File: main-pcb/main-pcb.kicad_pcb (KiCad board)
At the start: 10 copper layers, 12.8 x 6.5 mm, 428 parts, among them J1 CONN_01X03, J10 CONN_DUMPTRUCK_HOST, J11 CONN_01X03, J12 PMOD_HOST, J13 PMOD_HOST, J14 USB_C_Receptacle_USB2.0, J2 CORTEX_DEBUG_ETM, J3 XILINX_JTAG, J4 CORTEX_DEBUG_ETM, J5 CONN_01X03, J6 0826-1G1T-23-F, J7 CONN_DUMPTRUCK_HOST, J8 CONN_DUMPTRUCK_HOST, J9 CONN_DUMPTRUCK_HOST, M1 MECHANICAL, M2 SCREWHOLE, M3 SCREWHOLE, M4 SCREWHOLE, M5 SCREWHOLE, M6 MECHANICAL, M7 MECHANICAL, M8 MECHANICAL, M9 MECHANICAL, Q1 SSM6N58NU, SW1 SWITCH, SW2 SWITCH, U1 XC7S100-1FGGA484C, U10 NCP45525IMNTWG-H, U11 LTC3374-QFN, U12 AT24MAC402, U13 ECS-1612MV-250-CN, U14 STM32H735-UFBGA176-25, U15 S27KL0642GABHB020, U16 ECS-1612MV-250-CN, U17 S27KS0642GABHI030, U18 ECS-1612MV-250-CN, U19 INA230, U2 STM32L431-QFN48, U20 KSZ9031RN, U21 RCLAMP0514M, U22 RCLAMP0514M, U23 NCP45525IMNTWG-H, U24 IS25WP256D-JLLE, U25 INA230, U26 74LVC1T45, U27 NCP45525IMNTWG-H, U28 INA230, U29 NCP45525IMNTWG-H, U3 INA230, U30 INA230, U31 NCP45525IMNTWG-H, U32 INA230, U33 19-C47/RSGHBHC-5V01/2T, U34 19-C47/RSGHBHC-5V01/2T, U35 19-C47/RSGHBHC-5V01/2T, U36 19-C47/RSGHBHC-5V01/2T, U37 19-C47/RSGHBHC-5V01/2T, U38 19-C47/RSGHBHC-5V01/2T, U39 NCP45525IMNTWG-H, U4 INA230, U5 INA230, U6 INA230, U7 INA230, U8 INA230, U9 INA230

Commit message: Finished schematic review
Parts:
- added C208: 0.47 uF, azonenberg_pcb:EIA_0402_CAP_NOSILK, F.Cu at (38.3, 102.3)
- added TP18: GROUND, azonenberg_pcb:TESTPOINT_SMT_KEYSTONE_5016, F.Cu at (116.9, 43.2)
- added TP19: GROUND, azonenberg_pcb:TESTPOINT_SMT_KEYSTONE_5016, F.Cu at (116.9, 47.7)
- added TP20: GROUND, azonenberg_pcb:TESTPOINT_SMT_KEYSTONE_5016, F.Cu at (116.9, 52.1)
- R100, R96, R98: value 10K -> DNP
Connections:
- C100 pad 1: /Power supply/VBUS_SHOUT -> /VBUS_SHOUT
- C101 pad 1: /Power supply/VBUS_SHOUT -> /VBUS_SHOUT
- C166 pad 1: /Power supply/VBUS_SHOUT -> /VBUS_SHOUT
- C167 pad 1: /Power supply/VBUS_SHOUT -> /VBUS_SHOUT
- C169 pad 1: /Power supply/VBUS_SHOUT -> /VBUS_SHOUT
- C170 pad 1: /Power supply/VBUS_SHOUT -> /VBUS_SHOUT
- C171 pad 1: /Power supply/VBUS_SHOUT -> /VBUS_SHOUT
- C172 pad 1: /Power supply/VBUS_SHOUT -> /VBUS_SHOUT
- C173 pad 1: /Power supply/VBUS_SHOUT -> /VBUS_SHOUT
- C198 pad 1: /VBUS -> /VBUS_SHOUT
- C200 pad 1: /VBUS -> /VBUS_SHOUT
- C202 pad 1: /VBUS -> /VBUS_SHOUT
- C203 pad 1: /VBUS -> /VBUS_SHOUT
- C204 pad 1: /VBUS -> /VBUS_SHOUT
- C205 pad 1: /VBUS -> /VBUS_SHOUT
- C206 pad 1: /VBUS -> /VBUS_SHOUT
- C91 pad 1: /Power supply/VBUS_SHOUT -> /VBUS_SHOUT
- C93 pad 1: /Power supply/VBUS_SHOUT -> /VBUS_SHOUT
- C94 pad 1: /Power supply/VBUS_SHOUT -> /VBUS_SHOUT
- C96 pad 1: /Power supply/VBUS_SHOUT -> /VBUS_SHOUT
- C97 pad 1: /Power supply/VBUS_SHOUT -> /VBUS_SHOUT
- C98 pad 1: /Power supply/VBUS_SHOUT -> /VBUS_SHOUT
- J14 pad A6: Net-(J14-D+-PadA6) -> unconnected-(J14-D+-PadA6)
- J14 pad A7: Net-(J14-D--PadA7) -> unconnected-(J14-D--PadA7)
- J14 pad B6: Net-(J14-D+-PadA6) -> unconnected-(J14-D+-PadB6)
- J14 pad B7: Net-(J14-D--PadA7) -> unconnected-(J14-D--PadB7)
- R9 pad 1: /Power supply/VBUS_SHOUT -> /VBUS_SHOUT
- TP2 pad 1: /Power supply/VBUS_SHOUT -> /VBUS_SHOUT
- U11 pad 11: /Power supply/VBUS_SHOUT -> /VBUS_SHOUT
- U11 pad 13: /Power supply/VBUS_SHOUT -> /VBUS_SHOUT
- U11 pad 17: /Power supply/VBUS_SHOUT -> /VBUS_SHOUT
- U11 pad 2: /Power supply/VBUS_SHOUT -> /VBUS_SHOUT
- U11 pad 21: /Power supply/VBUS_SHOUT -> /VBUS_SHOUT
- U11 pad 24: /Power supply/VBUS_SHOUT -> /VBUS_SHOUT
- U11 pad 27: /Power supply/VBUS_SHOUT -> /VBUS_SHOUT
- U11 pad 30: /Power supply/VBUS_SHOUT -> /VBUS_SHOUT
- U11 pad 31: /Power supply/VBUS_SHOUT -> /VBUS_SHOUT
- U11 pad 35: /Power supply/VBUS_SHOUT -> /VBUS_SHOUT
- U11 pad 5: /Power supply/VBUS_SHOUT -> /VBUS_SHOUT
- U11 pad 6: /Power supply/VBUS_SHOUT -> /VBUS_SHOUT
- U11 pad 8: /Power supply/VBUS_SHOUT -> /VBUS_SHOUT
- U26 pad 6: /VBUS -> /VBUS_SHOUT
- U3 pad 11: /Power supply/VBUS_SHOUT -> /VBUS_SHOUT
- U3 pad 12: /Power supply/VBUS_SHOUT -> /VBUS_SHOUT
- U33 pad 2: /VBUS -> /VBUS_SHOUT
- U34 pad 2: /VBUS -> /VBUS_SHOUT
- U35 pad 2: /VBUS -> /VBUS_SHOUT
- U36 pad 2: /VBUS -> /VBUS_SHOUT
- U37 pad 2: /VBUS -> /VBUS_SHOUT
- U38 pad 2: /VBUS -> /VBUS_SHOUT

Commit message: First DUT socket fully routed
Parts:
- added C209: 47 uF, azonenberg_pcb:EIA_1210_CAP_NOSILK, F.Cu at (265.1, 66.9)
- added C210: 4.7 uF, azonenberg_pcb:EIA_0603_CAP_NOSILK, F.Cu at (264.2, 69.8)
- added C211: 4.7 uF, azonenberg_pcb:EIA_0603_CAP_NOSILK, F.Cu at (264.2, 71.6)
- added C212: 0.47 uF, azonenberg_pcb:EIA_0402_CAP_NOSILK, F.Cu at (261.3, 65.7)
- added C213: 0.47 uF, azonenberg_pcb:EIA_0402_CAP_NOSILK, F.Cu at (261.3, 67.2)
- added C214: 0.47 uF, azonenberg_pcb:EIA_0402_CAP_NOSILK, F.Cu at (261.3, 68.7)
- added C215: 0.47 uF, azonenberg_pcb:EIA_0402_CAP_NOSILK, F.Cu at (261.3, 70.2)
- C26, C27, C28, C29, C30, C31, C32, C33, C34, C40, C41, C42, C43, C44, C45, C55, C56, C57, C58, C59, C60, C62, C63, C67, C68, C69, C70, C75, C76, C77, C85, C86, C87, C88, C89, C90: moved to B.Cu
- moved C100 149.5 mm to (215.9, 41.9)
- moved C135 149.5 mm to (215.9, 44.5)
- moved C166 149.5 mm to (215.9, 47.1)
- moved C169 149.5 mm to (215.9, 49.7)
- moved C95 149.5 mm to (215.9, 39.3)
- moved C1 149.5 mm to (199.6, 38.8)
- moved C10 149.5 mm to (199.6, 50.8)
- moved C101 149.5 mm to (202.1, 46.3)
- moved C104 149.5 mm to (176.9, 77.2)
- moved C105 149.5 mm to (176.9, 79.0)
- moved C106 149.5 mm to (199.6, 60.9)
- moved C107 149.5 mm to (199.6, 63.5)
- moved C108 149.5 mm to (176.9, 80.8)
- moved C11 149.5 mm to (199.6, 52.3)
- moved C110 149.5 mm to (176.9, 82.6)
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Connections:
- U1 pad H2: /1V8 VCCIO socket/DUT_GPIO2 -> /1V8 VCCIO socket/DUT_GPIO40
- U1 pad H3: /1V8 VCCIO socket/DUT_GPIO4 -> /1V8 VCCIO socket/DUT_GPIO36
- U1 pad H4: /1V8 VCCIO socket/DUT_GPIO3 -> /1V8 VCCIO socket/DUT_GPIO38
- U1 pad H5: /1V8 VCCIO socket/DUT_GPIO10 -> /1V8 VCCIO socket/DUT_GPIO24
- U1 pad H6: /1V8 VCCIO socket/DUT_GPIO9 -> /1V8 VCCIO socket/DUT_GPIO26
- U1 pad H7: /1V8 VCCIO socket/DUT_GPIO0 -> /1V8 VCCIO socket/DUT_GPIO22
- U1 pad J1: /1V8 VCCIO socket/DUT_GPIO6 -> /1V8 VCCIO socket/DUT_GPIO46
- U1 pad J2: /1V8 VCCIO socket/DUT_GPIO5 -> /1V8 VCCIO socket/DUT_GPIO48
- U1 pad J3: /1V8 VCCIO socket/DUT_GPIO1 -> /1V8 VCCIO socket/DUT_GPIO34
- U1 pad J6: /1V8 VCCIO socket/DUT_GPIO12 -> /1V8 VCCIO socket/DUT_GPIO20
- U1 pad J7: /1V8 VCCIO socket/DUT_GPIO14 -> /1V8 VCCIO socket/DUT_GPIO18
- U1 pad J8: /1V8 VCCIO socket/DUT_GPIO13 -> /1V8 VCCIO socket/DUT_GPIO14
- U1 pad K1: /1V8 VCCIO socket/DUT_GPIO28 -> /1V8 VCCIO socket/DUT_GPIO42
- U1 pad K2: /1V8 VCCIO socket/DUT_GPIO8 -> /1V8 VCCIO socket/DUT_GPIO44
- U1 pad K3: /1V8 VCCIO socket/DUT_GPIO7 -> /1V8 VCCIO socket/DUT_GPIO41
- U1 pad K4: /1V8 VCCIO socket/DUT_GPIO20 -> /1V8 VCCIO socket/DUT_GPIO30
- U1 pad K5: /1V8 VCCIO socket/DUT_GPIO18 -> /1V8 VCCIO socket/DUT_GPIO32
- U1 pad K6: /1V8 VCCIO socket/DUT_GPIO11 -> /1V8 VCCIO socket/DUT_GPIO16
- U1 pad K8: /1V8 VCCIO socket/DUT_GPIO22 -> /1V8 VCCIO socket/DUT_GPIO12
- U1 pad L1: /1V8 VCCIO socket/DUT_GPIO27 -> /1V8 VCCIO socket/DUT_GPIO43
- U1 pad L4: /1V8 VCCIO socket/DUT_GPIO19 -> /1V8 VCCIO socket/DUT_GPIO28
- U1 pad L5: /1V8 VCCIO socket/DUT_GPIO17 -> /1V8 VCCIO socket/DUT_GPIO1
- U1 pad L6: /1V8 VCCIO socket/DUT_GPIO16 -> /1V8 VCCIO socket/DUT_GPIO0
- U1 pad L7: /1V8 VCCIO socket/DUT_GPIO15 -> /1V8 VCCIO socket/DUT_GPIO3
- U1 pad L8: /1V8 VCCIO socket/DUT_GPIO21 -> /1V8 VCCIO socket/DUT_GPIO10
- U1 pad M1: /1V8 VCCIO socket/DUT_GPIO30 -> /1V8 VCCIO socket/DUT_GPIO47
- U1 pad M2: /1V8 VCCIO socket/DUT_GPIO29 -> /1V8 VCCIO socket/DUT_GPIO49
- U1 pad M3: /1V8 VCCIO socket/DUT_GPIO26 -> /1V8 VCCIO socket/DUT_GPIO45
- U1 pad M4: /1V8 VCCIO socket/DUT_GPIO25 -> /1V8 VCCIO socket/DUT_GPIO27
- U1 pad M5: /1V8 VCCIO socket/DUT_GPIO40 -> /1V8 VCCIO socket/DUT_GPIO25
- U1 pad M7: /1V8 VCCIO socket/DUT_GPIO24 -> /1V8 VCCIO socket/DUT_GPIO5
- U1 pad M8: /1V8 VCCIO socket/DUT_GPIO23 -> /1V8 VCCIO socket/DUT_GPIO8
- U1 pad N1: /1V8 VCCIO socket/DUT_GPIO34 -> /1V8 VCCIO socket/DUT_GPIO39
- U1 pad N3: /1V8 VCCIO socket/DUT_GPIO32 -> /1V8 VCCIO socket/DUT_GPIO31
- U1 pad N4: /1V8 VCCIO socket/DUT_GPIO31 -> /1V8 VCCIO socket/DUT_GPIO29
- U1 pad N5: /1V8 VCCIO socket/DUT_GPIO39 -> /1V8 VCCIO socket/DUT_GPIO23
- U1 pad N6: /1V8 VCCIO socket/DUT_GPIO42 -> /1V8 VCCIO socket/DUT_GPIO17
- U1 pad N7: /1V8 VCCIO socket/DUT_GPIO44 -> /1V8 VCCIO socket/DUT_GPIO7
- U1 pad N8: /1V8 VCCIO socket/DUT_GPIO38 -> /1V8 VCCIO socket/DUT_GPIO6
- U1 pad P1: /1V8 VCCIO socket/DUT_GPIO33 -> /1V8 VCCIO socket/DUT_GPIO35
- U1 pad P2: /1V8 VCCIO socket/DUT_GPIO36 -> /1V8 VCCIO socket/DUT_GPIO37
- U1 pad P3: /1V8 VCCIO socket/DUT_GPIO35 -> /1V8 VCCIO socket/DUT_GPIO33
- U1 pad P6: /1V8 VCCIO socket/DUT_GPIO41 -> /1V8 VCCIO socket/DUT_GPIO13
- U1 pad P7: /1V8 VCCIO socket/DUT_GPIO43 -> /1V8 VCCIO socket/DUT_GPIO15
- U1 pad P8: /1V8 VCCIO socket/DUT_GPIO37 -> /1V8 VCCIO socket/DUT_GPIO4
- U1 pad R3: /1V8 VCCIO socket/DUT_GPIO49 -> /1V8 VCCIO socket/DUT_GPIO19
- U1 pad R4: /1V8 VCCIO socket/DUT_GPIO48 -> /1V8 VCCIO socket/DUT_GPIO21
- U1 pad R5: /1V8 VCCIO socket/DUT_GPIO47 -> /1V8 VCCIO socket/DUT_GPIO9
- U1 pad R6: /1V8 VCCIO socket/DUT_GPIO46 -> /1V8 VCCIO socket/DUT_GPIO11
- U1 pad R7: /1V8 VCCIO socket/DUT_GPIO45 -> /1V8 VCCIO socket/DUT_GPIO2
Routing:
- net /GND: track 0.00 -> 333.5 mm, vias 0 -> 115
- net /3V3: track 0.00 -> 81.4 mm, vias 0 -> 7
- net /1V8: track 0.00 -> 60.9 mm, vias 0 -> 18
- net /1V8 VCCIO socket/DUT_GPIO2: track 0.00 -> 46.2 mm, vias 0 -> 2
- net /1V8 VCCIO socket/DUT_GPIO4: track 0.00 -> 45.9 mm, vias 0 -> 2
- net /1V8 VCCIO socket/DUT_GPIO0: track 0.00 -> 41.6 mm, vias 0 -> 2
- net /1V8 VCCIO socket/DUT_GPIO3: track 0.00 -> 40.6 mm, vias 0 -> 2
- net /1V8 VCCIO socket/DUT_GPIO6: track 0.00 -> 40.6 mm, vias 0 -> 2
- net /1V8 VCCIO socket/DUT_GPIO1: track 0.00 -> 39.9 mm, vias 0 -> 2
- net /1V8 VCCIO socket/DUT_GPIO8: track 0.00 -> 39.4 mm, vias 0 -> 2
- net /1V8 VCCIO socket/DUT_GPIO5: track 0.00 -> 39.1 mm, vias 0 -> 2
- net /1V8 VCCIO socket/DUT_GPIO10: track 0.00 -> 37.9 mm, vias 0 -> 2
- net /1V8 VCCIO socket/DUT_GPIO7: track 0.00 -> 37.2 mm, vias 0 -> 2
- net /1V8 VCCIO socket/DUT_GPIO12: track 0.00 -> 36.4 mm, vias 0 -> 2
- net /1V8 VCCIO socket/DUT_GPIO11: track 0.00 -> 36.0 mm, vias 0 -> 2
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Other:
- board size 12.8 x 6.5 mm -> 133 x 90 mm

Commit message: Continued initial layout of 1.8V bank
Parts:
- C188, C189, C192, R98: moved to B.Cu
- moved C191 172.1 mm to (28.8, 79.5)
- moved U30 172.1 mm to (32.4, 80.8)
- moved C190 165.9 mm to (45.0, 74.0), turned to 180 degrees
- moved U29 162.0 mm to (48.2, 74.0), turned to 180 degrees
- moved C192 159.2 mm to (44.8, 81.0), turned to -90 degrees
- moved R99 157.4 mm to (46.0, 76.0), turned to 90 degrees
- moved C189 155.9 mm to (47.0, 73.2), turned to 90 degrees
- moved C188 153.1 mm to (49.5, 73.2), turned to 90 degrees
- moved R98 152.4 mm to (51.2, 74.7), turned to -90 degrees
- moved J2 81.5 mm to (132.5, 111.0)
- moved J12 54.8 mm to (109.7, 31.3), turned to 180 degrees
- moved J6 51.1 mm to (132.0, 36.5), turned to 0 degrees
- moved J4 20.0 mm to (91.0, 31.0)
- moved U21 19.3 mm to (134.5, 63.0), turned to 0 degrees
- moved U2 17.3 mm to (142.5, 81.5)
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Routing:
- net /1V8: track 60.9 -> 102.2 mm, vias 18 -> 22
- net /GND: track 333.5 -> 348.5 mm, vias 115 -> 123
- net /1V8 VCCIO socket/DUT_VCCIO_SHIN: track 0.00 -> 5.16 mm
- net /DUT_VCCIO_EN: track 0.00 -> 2.00 mm, vias 0 -> 1
- net /3V3: track 81.4 -> 82.7 mm, vias 7 -> 8
- net /1V8 VCCIO socket/DUT_VCCIO: track 6.40 -> 7.59 mm, vias 2 -> 0
- net /DUT_VDD: track 12.5 -> 13.4 mm, vias 4 -> 6
- net Net-(U29-SR): track 0.00 -> 0.25 mm, vias 0 -> 1
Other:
- board size 133 x 90 mm -> 123 x 90 mm

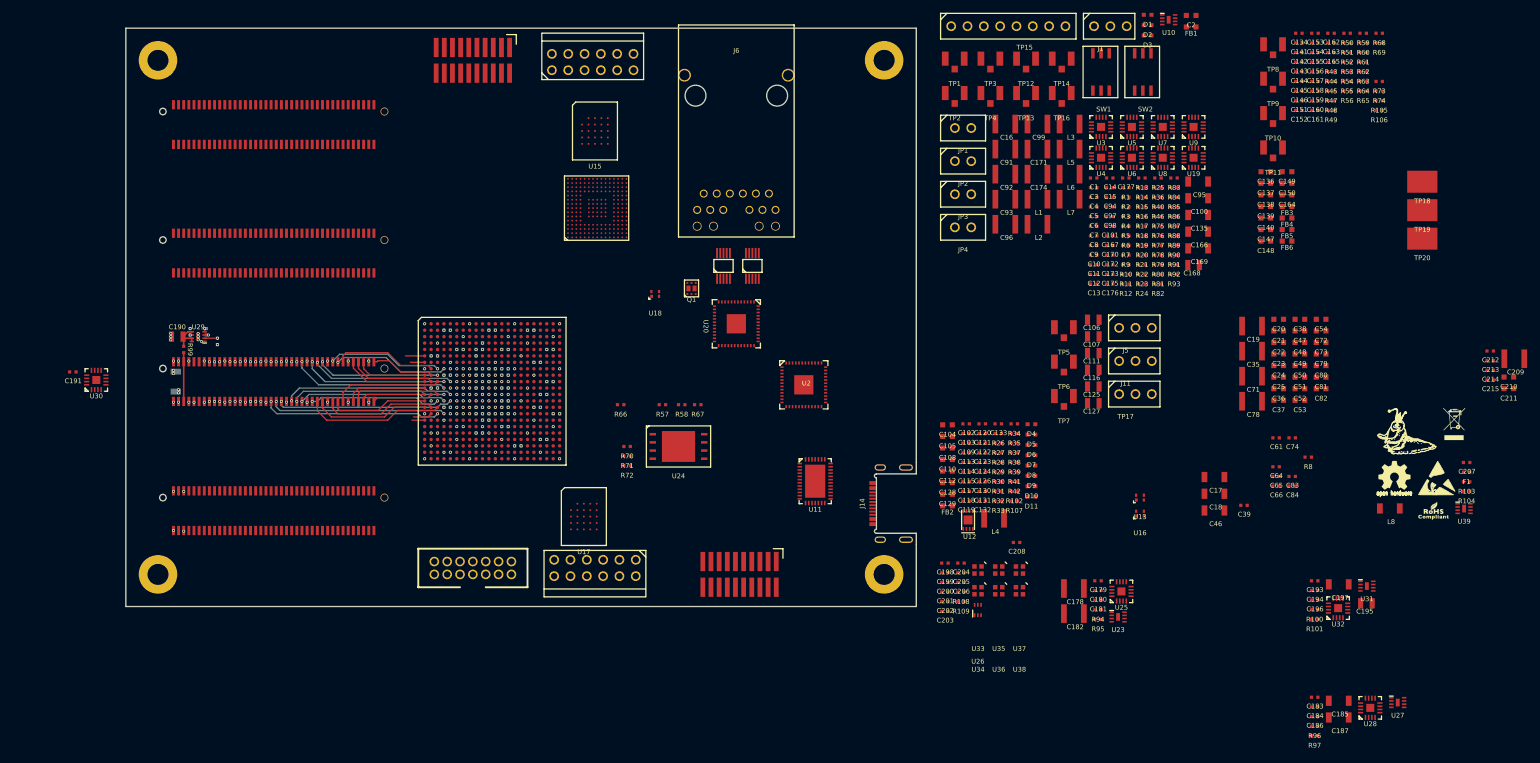
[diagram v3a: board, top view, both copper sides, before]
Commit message: Continued layout mostly of DUT connectors
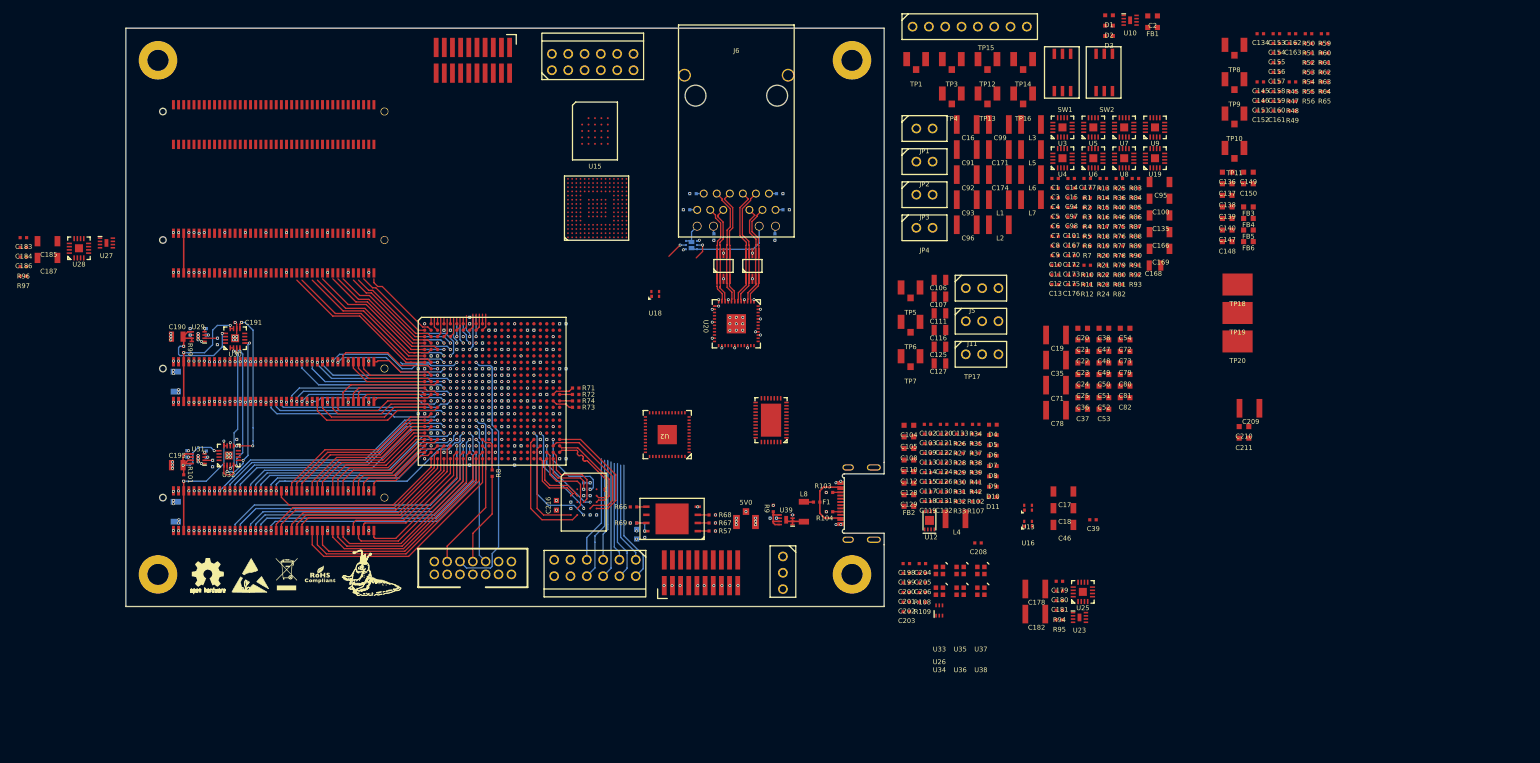
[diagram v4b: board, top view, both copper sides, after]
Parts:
- added C216: 4.7 uF, azonenberg_pcb:EIA_0603_CAP_NOSILK, F.Cu at (104.0, 100.2)
- added C217: 0.47 uF, azonenberg_pcb:EIA_0402_CAP_NOSILK, B.Cu at (108.8, 98.8)
- added C218: 0.47 uF, azonenberg_pcb:EIA_0402_CAP_NOSILK, B.Cu at (109.8, 101.8)
- added C219: 0.47 uF, azonenberg_pcb:EIA_0402_CAP_NOSILK, B.Cu at (106.2, 100.2)
- C141, C142, C143, C144, C164, C165, C193, C194, C196, C197, C207, C212, C213, C214, C215, C61, C64, C65, C66, C74, C83, C84, Q1, R100, R105, R106, R43, R44, R58, R70: moved to B.Cu
- R2, R3: value TBD -> 33K
- R29, R30, R31, R33, R34, R37, R38, R39: value 470 -> 33K
- R4: value TBD -> 4.7K
- moved U27 213.3 mm to (34.0, 59.4)
- moved U28 213.3 mm to (29.7, 60.2)
- moved C183 213.3 mm to (21.1, 58.6)
- moved C184 213.3 mm to (21.1, 60.1)
- moved C185 213.3 mm to (24.8, 59.1)
- moved C186 213.3 mm to (21.1, 61.6)
- moved C187 213.3 mm to (24.8, 61.7)
- moved R96 213.3 mm to (21.1, 63.1)
- moved R97 213.3 mm to (21.1, 64.6)
- moved C195 186.3 mm to (45.0, 94.0), turned to 180 degrees
- moved M7 185.3 mm to (49.8, 110.7)
- moved M6 185.3 mm to (56.5, 111.2)
- moved M9 183.2 mm to (62.0, 111.0)
- moved U31 183.0 mm to (48.2, 93.0), turned to 180 degrees
- moved C197 181.4 mm to (44.8, 101.2), turned to -90 degrees
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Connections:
- U1 pad AA1: /1V2 VCCIO socket/DUT_GPIO34 -> /1V2 VCCIO socket/DUT_GPIO46
- U1 pad AA10: /1V2 VCCIO socket/DUT_GPIO43 -> /1V2 VCCIO socket/DUT_GPIO33
- U1 pad AA2: /1V2 VCCIO socket/DUT_GPIO33 -> /1V2 VCCIO socket/DUT_GPIO48
- U1 pad AA20: /Ethernet/FPGA_RAM_DQ6 -> /Ethernet/FPGA_RAM_DQ1
- U1 pad AA21: /Ethernet/ETH_LED2_N_1V8_INV -> /Ethernet/FPGA_RAM_DQS
- U1 pad AA22: /Ethernet/ETH_LED1_N_1V8 -> /Ethernet/FPGA_RAM_PSC_P
- U1 pad AA3: /1V2 VCCIO socket/DUT_GPIO30 -> /1V2 VCCIO socket/DUT_GPIO21
- U1 pad AA6: /1V2 VCCIO socket/DUT_GPIO25 -> /1V2 VCCIO socket/DUT_GPIO47
- U1 pad AA8: /1V2 VCCIO socket/DUT_GPIO40 -> /1V2 VCCIO socket/DUT_GPIO39
- U1 pad AA9: /1V2 VCCIO socket/DUT_GPIO47 -> /1V2 VCCIO socket/DUT_GPIO37
- U1 pad AB10: /1V2 VCCIO socket/DUT_GPIO44 -> /1V2 VCCIO socket/DUT_GPIO31
- U1 pad AB19: unconnected-(U1E-IO_L23P_T3_D19_14-PadAB19) -> /Ethernet/FPGA_RAM_CLK_N
- U1 pad AB2: /1V2 VCCIO socket/DUT_GPIO32 -> /1V2 VCCIO socket/DUT_GPIO22
- U1 pad AB20: unconnected-(U1E-IO_L23N_T3_D18_14-PadAB20) -> /Ethernet/FPGA_RAM_CLK_P
- U1 pad AB21: unconnected-(U1E-IO_L22N_T3_D20_14-PadAB21) -> /Ethernet/FPGA_RAM_CS_N
- U1 pad AB3: /1V2 VCCIO socket/DUT_GPIO31 -> /1V2 VCCIO socket/DUT_GPIO23
- U1 pad AB4: /1V2 VCCIO socket/DUT_GPIO36 -> /1V2 VCCIO socket/DUT_GPIO27
- U1 pad AB5: /1V2 VCCIO socket/DUT_GPIO35 -> /1V2 VCCIO socket/DUT_GPIO43
- U1 pad AB6: /1V2 VCCIO socket/DUT_GPIO26 -> /1V2 VCCIO socket/DUT_GPIO49
- U1 pad AB7: /1V2 VCCIO socket/DUT_GPIO46 -> /1V2 VCCIO socket/DUT_GPIO41
- U1 pad AB9: /1V2 VCCIO socket/DUT_GPIO48 -> /1V2 VCCIO socket/DUT_GPIO35
- U1 pad P17: /Ethernet/FPGA_RAM_CLK_P -> /Ethernet/ETH_RST_N
- U1 pad R16: /Ethernet/FPGA_RAM_DQS -> unconnected-(U1E-IO_L16P_T2_CSI_B_14-PadR16)
- U1 pad R17: /Ethernet/FPGA_RAM_DQ0 -> /Ethernet/ETH_LED2_N_1V8_INV
- U1 pad R18: /Ethernet/FPGA_RAM_CLK_N -> unconnected-(U1E-IO_L14N_T2_SRCC_14-PadR18)
- U1 pad R19: /Ethernet/FPGA_RAM_DQ1 -> /Ethernet/ETH_LED1_N_1V8_INV
- U1 pad R2: /1V2 VCCIO socket/DUT_GPIO0 -> /1V2 VCCIO socket/DUT_GPIO24
- U1 pad R20: /Ethernet/FPGA_RAM_DQ2 -> /Ethernet/ETH_LED1_N_1V8
- U1 pad T1: /1V2 VCCIO socket/DUT_GPIO49 -> /1V2 VCCIO socket/DUT_GPIO26
- U1 pad T17: /Ethernet/FPGA_RAM_CS_N -> unconnected-(U1E-IO_L15P_T2_DQS_RDWR_B_14-PadT17)
- U1 pad T19: /Ethernet/FPGA_RAM_DQ3 -> unconnected-(U1E-IO_L18P_T2_D28_14-PadT19)
- U1 pad T2: /1V2 VCCIO socket/DUT_GPIO24 -> /1V2 VCCIO socket/DUT_GPIO28
- U1 pad T20: /Ethernet/FPGA_RAM_DQ4 -> unconnected-(U1E-IO_L18N_T2_D27_14-PadT20)
- U1 pad T3: /1V2 VCCIO socket/DUT_GPIO23 -> /1V2 VCCIO socket/DUT_GPIO4
- U1 pad T5: /1V2 VCCIO socket/DUT_GPIO7 -> /1V2 VCCIO socket/DUT_GPIO2
- U1 pad T6: /1V2 VCCIO socket/DUT_GPIO4 -> /1V2 VCCIO socket/DUT_GPIO0
- U1 pad T7: /1V2 VCCIO socket/DUT_GPIO3 -> /1V2 VCCIO socket/DUT_GPIO1
- U1 pad T8: /1V2 VCCIO socket/DUT_GPIO11 -> /1V2 VCCIO socket/DUT_GPIO5
- U1 pad U1: /1V2 VCCIO socket/DUT_GPIO18 -> /1V2 VCCIO socket/DUT_GPIO30
- U1 pad U17: /Ethernet/FPGA_RAM_RST_N -> /Ethernet/ETH_LED2_N_1V8
- U1 pad U2: /1V2 VCCIO socket/DUT_GPIO17 -> /1V2 VCCIO socket/DUT_GPIO32
- U1 pad U20: /Ethernet/FPGA_RAM_PSC_P -> unconnected-(U1E-IO_L11P_T1_SRCC_14-PadU20)
- U1 pad U3: /1V2 VCCIO socket/DUT_GPIO22 -> /1V2 VCCIO socket/DUT_GPIO8
- U1 pad U4: /1V2 VCCIO socket/DUT_GPIO21 -> /1V2 VCCIO socket/DUT_GPIO6
- U1 pad U5: /1V2 VCCIO socket/DUT_GPIO8 -> /1V2 VCCIO socket/DUT_GPIO3
- U1 pad U8: /1V2 VCCIO socket/DUT_GPIO12 -> /1V2 VCCIO socket/DUT_GPIO7
- U1 pad V1: /1V2 VCCIO socket/DUT_GPIO13 -> /1V2 VCCIO socket/DUT_GPIO34
- U1 pad V18: unconnected-(U1E-IO_L24P_T3_D17_14-PadV18) -> /Ethernet/FPGA_RAM_DQ5
- U1 pad V19: unconnected-(U1E-IO_L24N_T3_D16_14-PadV19) -> /Ethernet/FPGA_RAM_DQ0
- U1 pad V20: /Ethernet/FPGA_RAM_PSC_N -> /Ethernet/RGMII_TXD3
- U1 pad V4: /1V2 VCCIO socket/DUT_GPIO6 -> /1V2 VCCIO socket/DUT_GPIO10
- U1 pad V5: /1V2 VCCIO socket/DUT_GPIO5 -> /1V2 VCCIO socket/DUT_GPIO12
- U1 pad V6: /1V2 VCCIO socket/DUT_GPIO10 -> /1V2 VCCIO socket/DUT_GPIO18
- U1 pad V7: /1V2 VCCIO socket/DUT_GPIO9 -> /1V2 VCCIO socket/DUT_GPIO20
- U1 pad V8: /1V2 VCCIO socket/DUT_GPIO37 -> /1V2 VCCIO socket/DUT_GPIO19
- U1 pad W1: /1V2 VCCIO socket/DUT_GPIO14 -> /1V2 VCCIO socket/DUT_GPIO38
- U1 pad W18: /Ethernet/ETH_LED2_N_1V8 -> /Ethernet/FPGA_RAM_DQ6
- U1 pad W2: /1V2 VCCIO socket/DUT_GPIO15 -> /1V2 VCCIO socket/DUT_GPIO36
- U1 pad W21: unconnected-(U1E-IO_L10P_T1_D14_14-PadW21) -> /Ethernet/FPGA_RAM_RST_N
- U1 pad W22: /Ethernet/RGMII_TXD3 -> /Ethernet/FPGA_RAM_DQ4
- U1 pad W3: /1V2 VCCIO socket/DUT_GPIO19 -> /1V2 VCCIO socket/DUT_GPIO40
- U1 pad W4: /1V2 VCCIO socket/DUT_GPIO2 -> /1V2 VCCIO socket/DUT_GPIO14
- U1 pad W5: /1V2 VCCIO socket/DUT_GPIO1 -> /1V2 VCCIO socket/DUT_GPIO16
- U1 pad W7: /1V2 VCCIO socket/DUT_GPIO41 -> /1V2 VCCIO socket/DUT_GPIO11
- U1 pad W8: /1V2 VCCIO socket/DUT_GPIO38 -> /1V2 VCCIO socket/DUT_GPIO15
- U1 pad Y1: /1V2 VCCIO socket/DUT_GPIO16 -> /1V2 VCCIO socket/DUT_GPIO42
- U1 pad Y19: /Ethernet/ETH_LED1_N_1V8_INV -> /Ethernet/FPGA_RAM_DQ7
- U1 pad Y20: /Ethernet/FPGA_RAM_DQ5 -> /Ethernet/FPGA_RAM_DQ2
- U1 pad Y21: /Ethernet/ETH_RST_N -> /Ethernet/FPGA_RAM_DQ3
- U1 pad Y22: /Ethernet/FPGA_RAM_DQ7 -> /Ethernet/FPGA_RAM_PSC_N
- U1 pad Y3: /1V2 VCCIO socket/DUT_GPIO20 -> /1V2 VCCIO socket/DUT_GPIO44
- U1 pad Y4: /1V2 VCCIO socket/DUT_GPIO29 -> /1V2 VCCIO socket/DUT_GPIO25
- U1 pad Y5: /1V2 VCCIO socket/DUT_GPIO28 -> /1V2 VCCIO socket/DUT_GPIO29
- U1 pad Y6: /1V2 VCCIO socket/DUT_GPIO27 -> /1V2 VCCIO socket/DUT_GPIO9
- U1 pad Y7: /1V2 VCCIO socket/DUT_GPIO42 -> /1V2 VCCIO socket/DUT_GPIO13
- U1 pad Y8: /1V2 VCCIO socket/DUT_GPIO39 -> /1V2 VCCIO socket/DUT_GPIO17
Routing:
- net /GND: track 348.5 -> 863.3 mm, vias 123 -> 233
- net /3V3: track 82.7 -> 225.5 mm, vias 8 -> 15
- net /1V2: track 8.12 -> 99.4 mm, vias 3 -> 8
- net /PRSNT_2V5: track 0.00 -> 64.8 mm, vias 0 -> 1
- net /1V8: track 102.2 -> 164.1 mm, vias 22 -> 36
- net /I2C_SDA: track 0.00 -> 57.9 mm, vias 0 -> 3
- net /I2C_SCL: track 0.00 -> 51.2 mm, vias 0 -> 3
- net /1V2 VCCIO socket/DUT_GPIO1: track 0.00 -> 47.4 mm, vias 0 -> 2
- net /1V2 VCCIO socket/DUT_GPIO5: track 0.00 -> 47.0 mm, vias 0 -> 2
- net /1V2 VCCIO socket/DUT_GPIO7: track 0.00 -> 44.6 mm, vias 0 -> 2
- net /1V2 VCCIO socket/DUT_GPIO11: track 0.00 -> 44.5 mm, vias 0 -> 2
- net /1V2 VCCIO socket/DUT_GPIO3: track 0.00 -> 44.3 mm, vias 0 -> 2
- net /1V2 VCCIO socket/DUT_GPIO9: track 0.00 -> 43.7 mm, vias 0 -> 2
- net /1V2 VCCIO socket/DUT_GPIO19: track 0.00 -> 43.6 mm, vias 0 -> 2
- net /1V2 VCCIO socket/DUT_GPIO15: track 0.00 -> 43.4 mm, vias 0 -> 2
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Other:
- board size 123 x 90 mm -> 118 x 90 mm
- board text added: "5V0"
